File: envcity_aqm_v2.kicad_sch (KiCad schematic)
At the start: 137 parts, among them IC1 DS1307ZN+, IC2 DMMT5401-7F, IC3 DMMT5401-7F, IC4 DMMT5401-7-F, IC6 ESP32-S2-SOLO-N4R2, J1 USB_B_Micro, J10 Conn_01x06_Male, J11 Conn_01x06_Male, J12 Conn_01x06_Male, J13 Conn_01x06_Male, J14 Conn_01x08_Pin, J15 Conn_01x02_Male, J16 Conn_01x02_Male, J2 Screw_Terminal_01x02, J3 Screw_Terminal_01x02, J4 Micro_SD_Card, J5 Conn_01x03_Male, J6 Conn_01x04_Male, J7 Conn_01x06_Pin, J8 Conn_01x06_Male, J9 Conn_01x06_Male, Q1 DMG2301L / DMP2045U, Q2 DMG2301L / DMP2045U, Q3 DMG2301L, Q4 DMG2301L, Q5 DMG2301L / DMP2045U, Q6 DMG2301L, Q7 DMN10H220L, Q8 DMN10H220L, SW1 BOOT, SW1 RESET, U1 TP4056, U10 RFM95W-915S2, U11 ADS1115IDGS, U2 USBLC6-2SC6, U3 MT3608, U4 MT3608, U5 LM2596S-5, U6 AP2112K-3.3, U7 DHT11, U8 AP2112K-3.3, U9 CD74HC4067M, Y1 32,768KHz

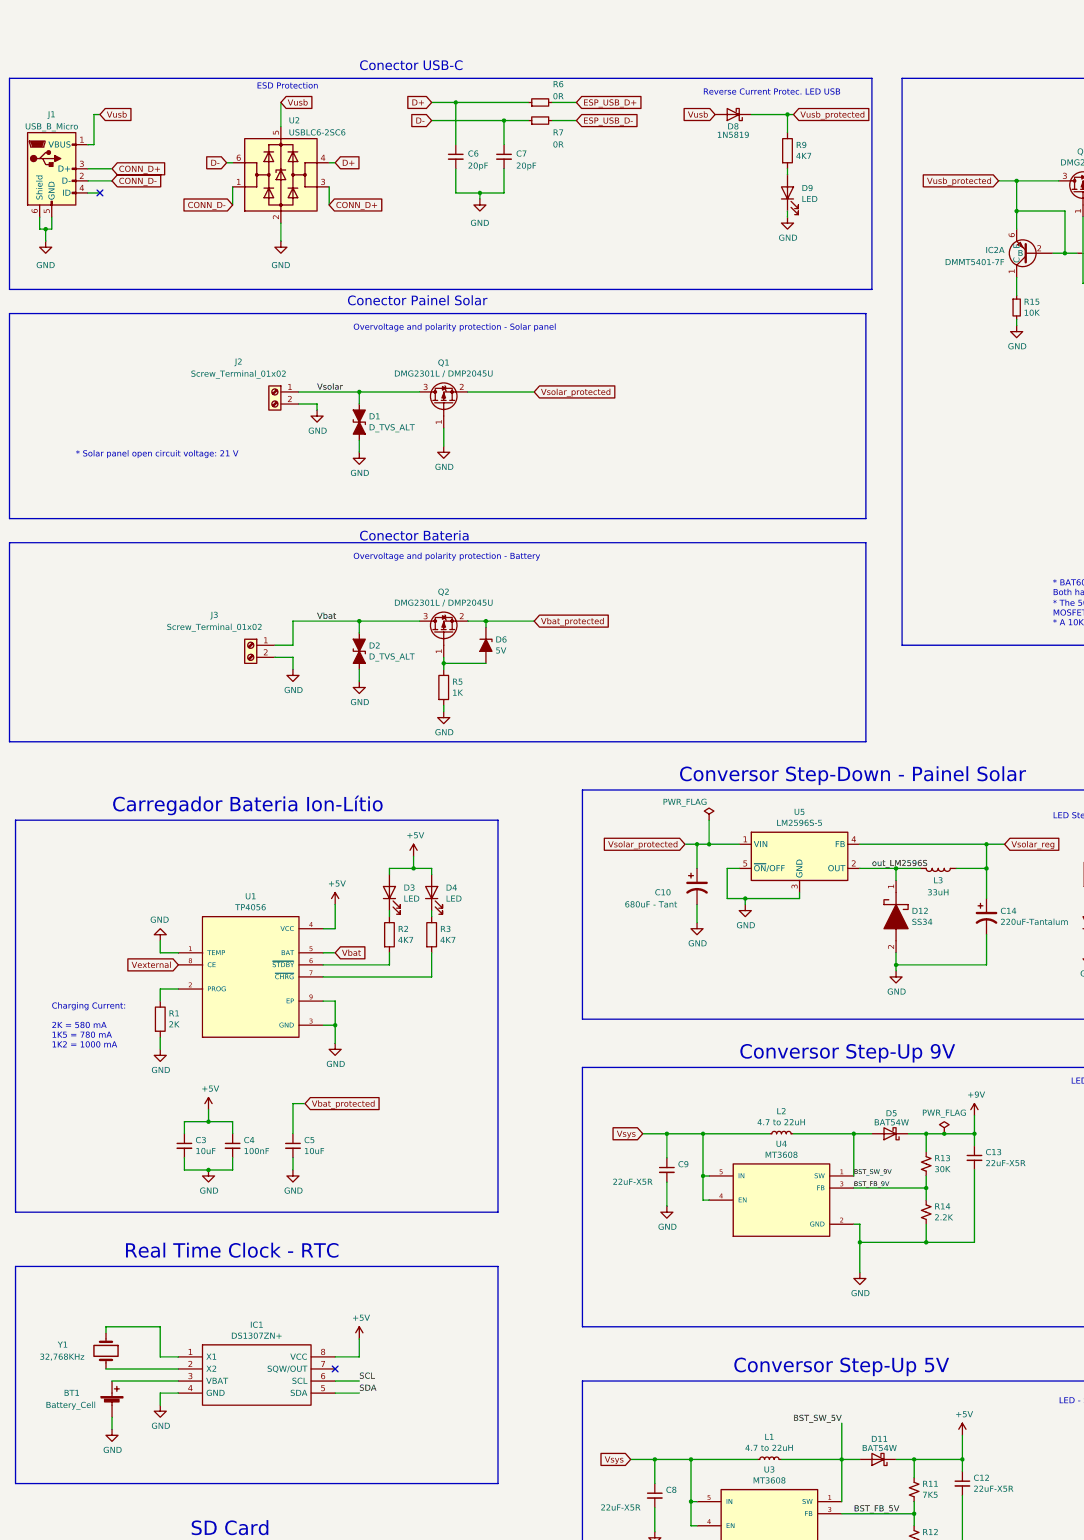
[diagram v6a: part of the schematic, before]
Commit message: Alterando os indutores. Add diversos 3dmodel. Alterando cristal rtc. Refaz algumas trilhas
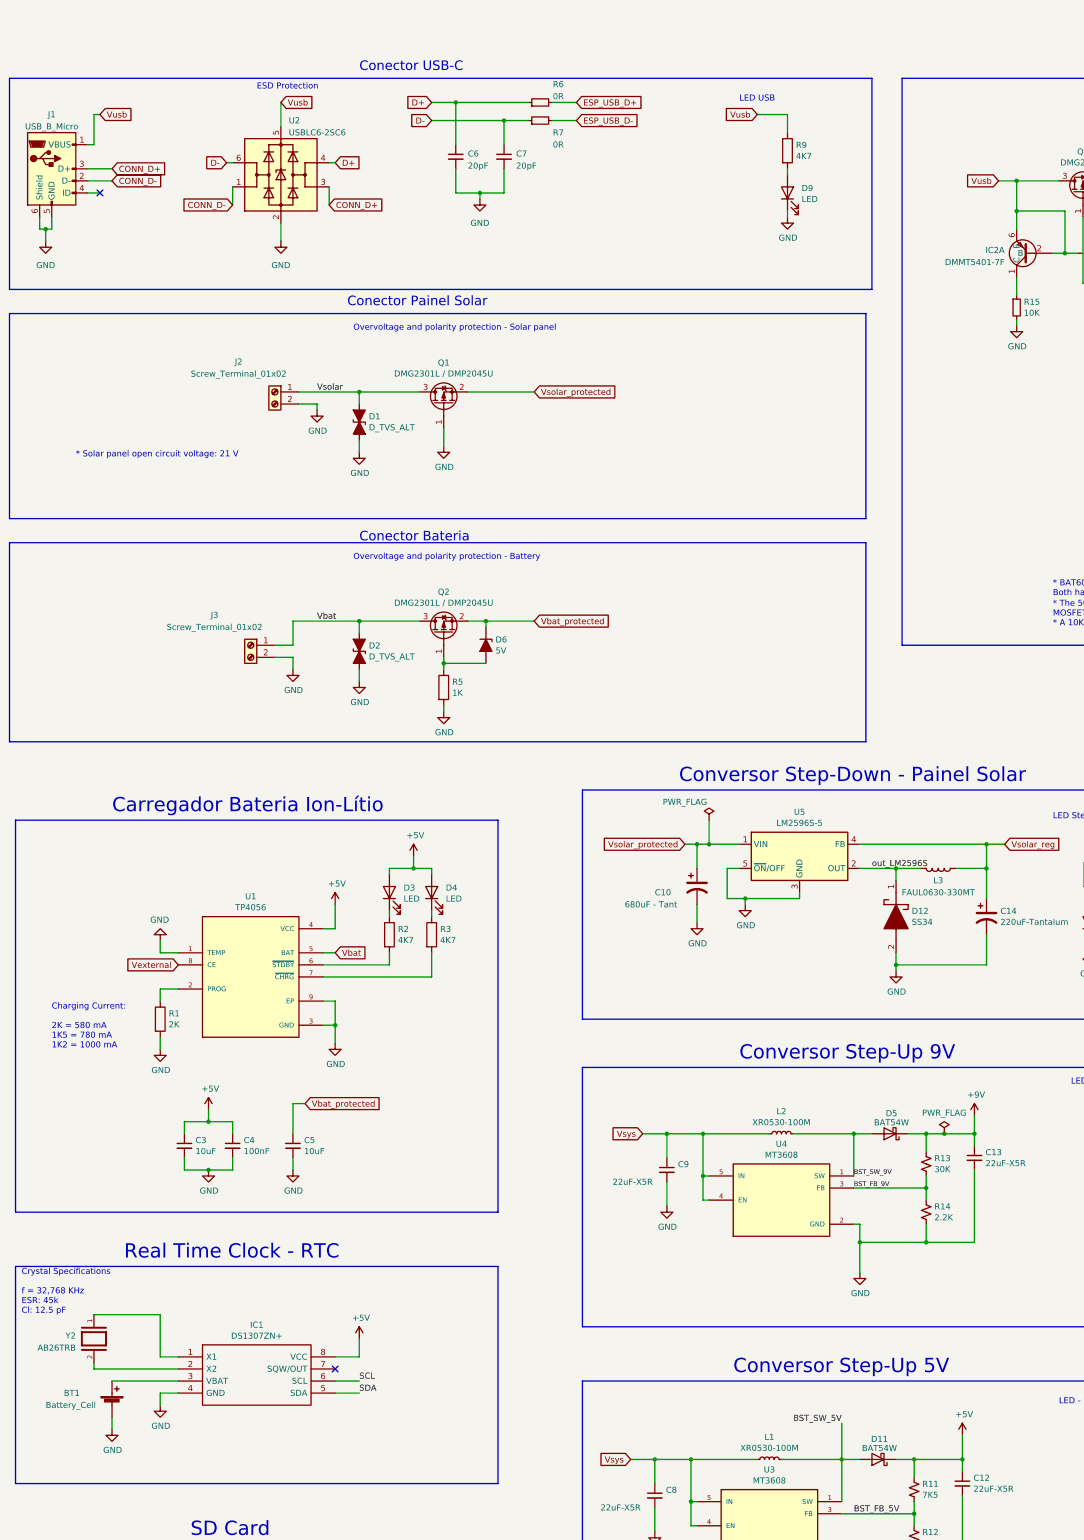
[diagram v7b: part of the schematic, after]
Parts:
- removed D8: 1N5819, Diode_THT:D_DO-41_SOD81_P10.16mm_Horizontal, symbol Diode:1N5819
- removed Y1: 32,768KHz, Crystal:Crystal_AT310_D3.0mm_L10.0mm_Horizontal, symbol Device:Crystal
- added Y2: AB26TRB, AB26TRB-32.768KHZ-T:XTAL_AB26TRB-32.768KHZ-T, symbol AB26TRB-32.768KHZ-T:AB26TRB-32.768KHZ-T
- C1, C2: footprint Capacitor_SMD:C_0805_2012Metric -> Capacitor_SMD:C_0603_1608Metric
- D12: footprint SamacSys_Parts:DIOM8059X256N -> Diode_SMD:D_SMB; LCSC Part# (none) -> C1884574
- L1, L2: value 4.7 to 22uH -> XR0530-100M; footprint Inductor_SMD:L_Wuerth_HCI-1040 -> Inductor_SMD:L_Chilisin_BMRA00050530; LCSC Part# (none) -> C5307602
- L3: value 33uH -> FAUL0630-330MT; footprint Inductor_SMD:L_Wuerth_HCI-1040 -> FDSD0630-H-1R0M_P3:IND_FDSD0630-H-1R0M=P3; LCSC Part# (none) -> C3040360
- R11, R12, R35, R36: footprint Resistor_SMD:R_0805_2012Metric -> Resistor_SMD:R_0603_1608Metric
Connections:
- net Vusb_protected is gone; now on net Vusb: IC2.2 (B), IC2.3 (B), IC2.6 (E), Q3.3 (D), R9.1
- net at IC1.1 (X1): now also Y2.1
- net at IC1.2 (X2): now also Y2.2
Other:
- note added: "Crystal Specifications f = 32,768 KHz ESR: 45k Cl: 12.5 pF"
- note added: "LED USB"
- note removed: "Reverse Current Protec. LED USB"

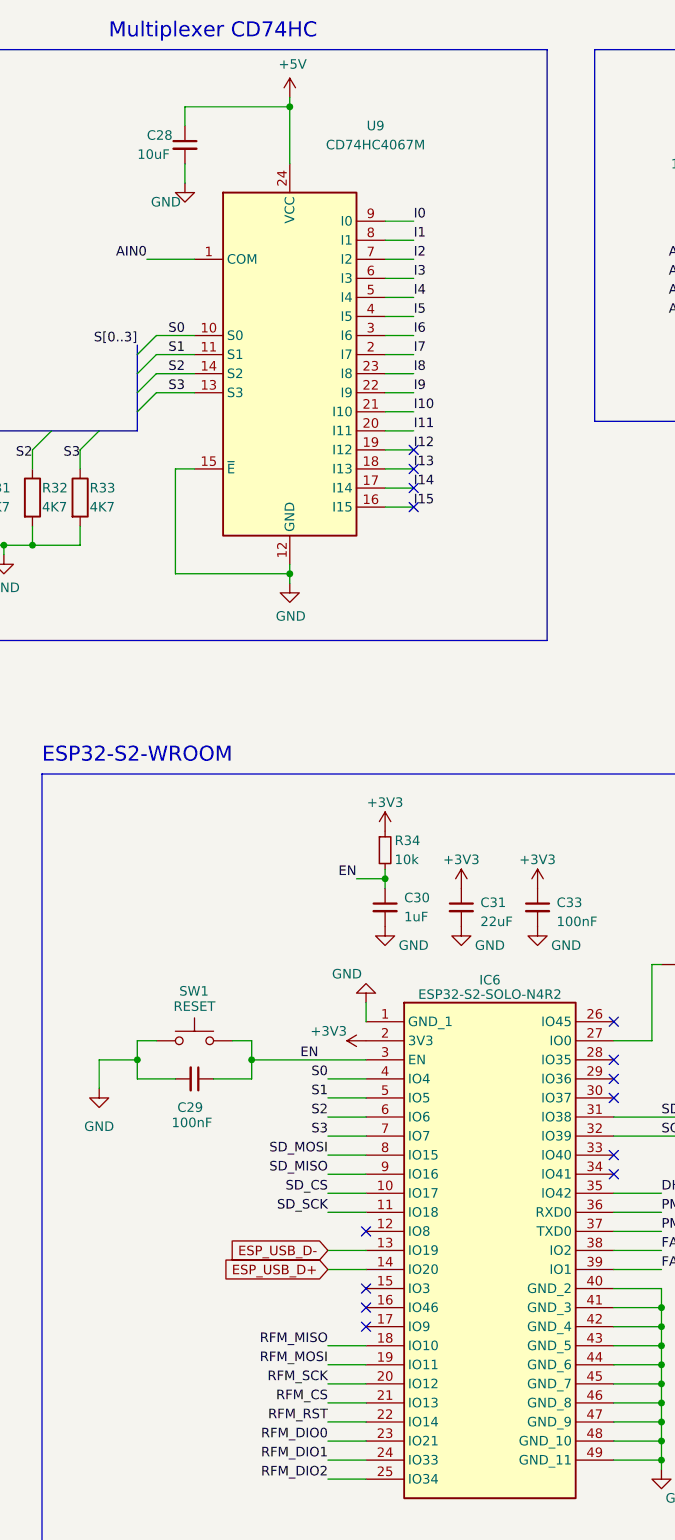
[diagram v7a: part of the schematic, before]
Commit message: Roteamento do cartao sd (incompleto). Roteamento USB com controle de impedancia ok.
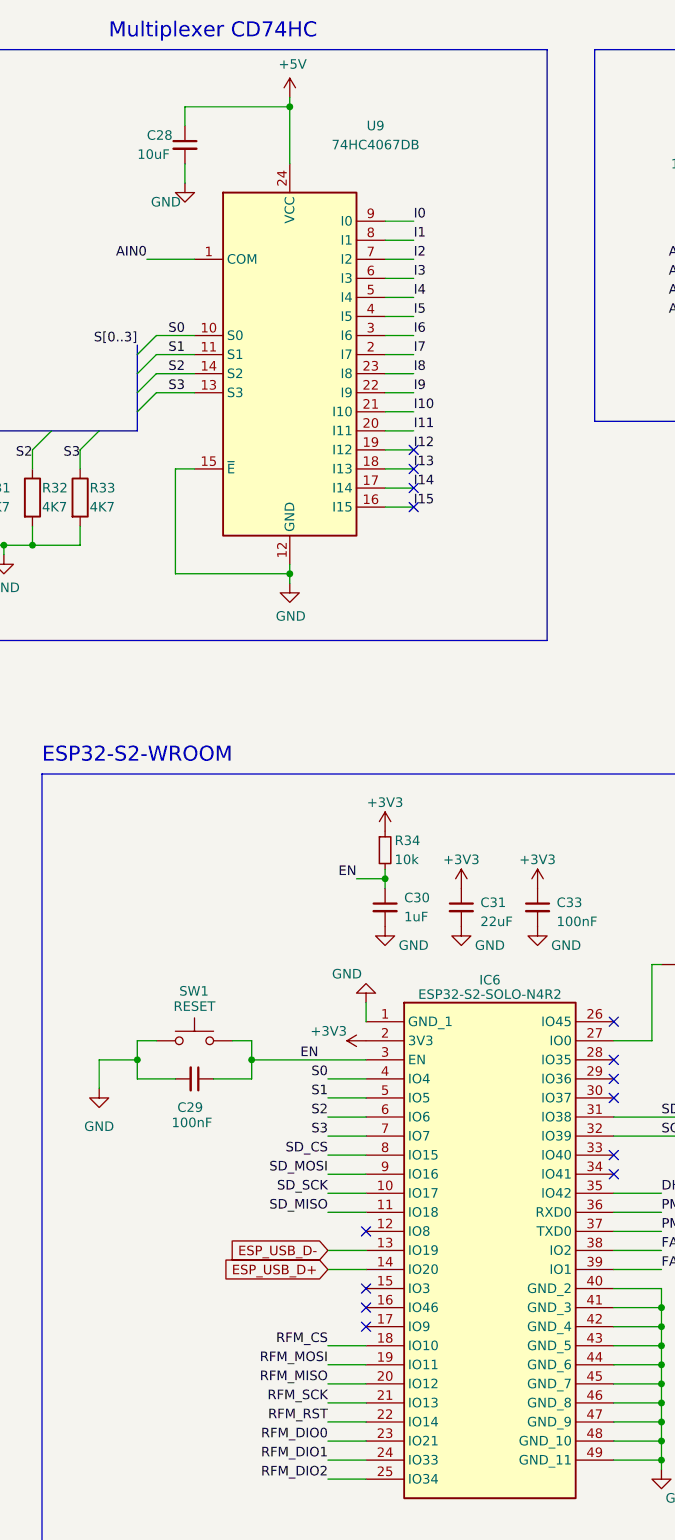
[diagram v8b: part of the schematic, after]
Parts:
- IC6: LCSC Part# (none) -> C3040594
- U9: value CD74HC4067M -> 74HC4067DB; footprint Package_SO:SOIC-24W_7.5x15.4mm_P1.27mm -> Package_SO:SSOP-24_5.3x8.2mm_P0.65mm; LCSC Part# (none) -> C124924
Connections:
- net RFM_CS: now also IC6.18 (IO10); no longer IC6.21 (IO13)
- net RFM_MISO: now also IC6.20 (IO12); no longer IC6.18 (IO10)
- net RFM_SCK: now also IC6.21 (IO13); no longer IC6.20 (IO12)
- net SD_CS: now also IC6.8 (IO15); no longer IC6.10 (IO17)
- net SD_MISO: now also IC6.11 (IO18); no longer IC6.9 (IO16)
- net SD_MOSI: now also IC6.9 (IO16); no longer IC6.8 (IO15)
- net SD_SCK: now also IC6.10 (IO17); no longer IC6.11 (IO18)
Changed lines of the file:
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@@
     (effects (font (size 1.27 1.27)) (justify left bottom))
   )
-  (label "SD_SCK" (at 457.2 177.8 180) (fields_autoplaced)
+  (label "SD_SCK" (at 457.2 175.26 180) (fields_autoplaced)
     (effects (font (size 1.27 1.27)) (justify right bottom))
   )
@@
     (effects (font (size 1.27 1.27)) (justify left bottom))
   )
-  (label "RFM_SCK" (at 457.2 200.66 180) (fields_autoplaced)
+  (label "RFM_SCK" (at 457.2 203.2 180) (fields_autoplaced)
     (effects (font (size 1.27 1.27)) (justify right bottom))
   )
@@
     (effects (font (size 1.27 1.27)) (justify right bottom))
   )
-  (label "RFM_MISO" (at 457.2 195.58 180) (fields_autoplaced)
+  (label "RFM_MISO" (at 457.2 200.66 180) (fields_autoplaced)
     (effects (font (size 1.27 1.27)) (justify right bottom))
   )
@@
     (effects (font (size 1.27 1.27)) (justify right bottom))
   )
-  (label "SD_MOSI" (at 457.2 170.18 180) (fields_autoplaced)
+  (label "SD_MOSI" (at 457.2 172.72 180) (fields_autoplaced)
     (effects (font (size 1.27 1.27)) (justify right bottom))
   )
@@
     (effects (font (size 1.27 1.27)) (justify left bottom))
   )
-  (label "SD_MISO" (at 457.2 172.72 180) (fields_autoplaced)
+  (label "SD_MISO" (at 457.2 177.8 180) (fields_autoplaced)
     (effects (font (size 1.27 1.27)) (justify right bottom))
   )
@@
     (effects (font (size 1.27 1.27)) (justify left bottom))
   )
-  (label "SD_CS" (at 457.2 175.26 180) (fields_autoplaced)
+  (label "SD_CS" (at 457.2 170.18 180) (fields_autoplaced)
     (effects (font (size 1.27 1.27)) (justify right bottom))
   )
@@
     (effects (font (size 1.27 1.27)) (justify right bottom))
   )
-  (label "RFM_CS" (at 457.2 203.2 180) (fields_autoplaced)
+  (label "RFM_CS" (at 457.2 195.58 180) (fields_autoplaced)
     (effects (font (size 1.27 1.27)) (justify right bottom))
   )
@@
       (effects (font (size 1.27 1.27)))
     )
-    (property "Value" "CD74HC4067M" (at 463.55 35.56 0)
+    (property "Value" "74HC4067DB" (at 463.55 35.56 0)
       (effects (font (size 1.27 1.27)))
     )
-    (property "Footprint" "Package_SO:SOIC-24W_7.5x15.4mm_P1.27mm" (at 474.98 88.9 0)
+    (property "Footprint" "Package_SO:SSOP-24_5.3x8.2mm_P0.65mm" (at 474.98 88.9 0)
       (effects (font (size 1.27 1.27) italic) hide)
     )
@@
       (effects (font (size 1.27 1.27)) hide)
     )
+    (property "LCSC Part#" "C124924" (at 452.12 63.5 0)
+      (effects (font (size 1.27 1.27)) hide)
+    )
     (pin "1")
     (pin "10")
@@
       (effects (font (size 1.27 1.27)) (justify left top) hide)
     )
+    (property "LCSC Part#" "C3040594" (at 462.28 152.4 0)
+      (effects (font (size 1.27 1.27)) hide)
+    )
     (pin "1")
